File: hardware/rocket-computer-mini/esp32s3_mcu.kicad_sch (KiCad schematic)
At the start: 35 parts, among them SW3 R-667995, U11 GD5F2GQ5UEYIGR, U13 W25Q128JVSIQ, U14 479480001, U15 ESP32-S3RH2, Y1 ABS07-32.768KHZ-T, Y2 ECS-400-10-37B2-CKY-TR

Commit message: hardware: rename the External Connections sheet to Pyro, wire up the 3D models
Two changes that both needed the KiCad session closed.

The External Connections sheet becomes Pyro, in pyro.kicad_sch. The old name
described a sheet that carried the expansion header, camera, servo and piezo
alongside the pyro channels; all of those were removed during the reduction, so
the sheet now carries the four pyro channels and little else. Renamed in the root
schematic, in the project file's sheet list, and across 78 footprint sheetname
and sheetfile properties in the PCB, with the file moved to match.

The two 3D models added earlier are now referenced from their footprints, at
zero offset and rotation -- both were drawn at the footprint origin so they need
no transform. Paths resolve through ${KIPRJMOD}/../3dmodels/ like the other 63.

Verified: the netlist exports cleanly at 157 parts and the sheet path now reads
/Pyro/ alongside /Sensors/, /Power/ and /MCU - ESP32-S3/. No reference to the old
name survives anywhere in the board directory.

Note on the DRC numbers, which look alarming and are not from this change: the
board file currently holds zero net declarations and zero track segments, so DRC
reports every connection as missing. The layout has not been resynced since the
processor removal. That is known and separate.

Also corrects the README, which still described the sheet set as it stood at the
fork.

Co-Authored-By: Claude Opus 5 <noreply@anthropic.com>
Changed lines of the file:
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@@
+		)
+	)
+	(global_label "L_RXEN"
+		(shape input)
+		(at 161.925 86.36 180)
+		(fields_autoplaced yes)
+		(effects
+			(font
+				(size 1.27 1.27)
+			)
+			(justify right)
+		)
+		(property "Intersheetrefs" "${INTERSHEET_REFS}"
+			(at 150.4127 86.36 180)
+			(hide yes)
+			(show_name no)
+			(do_not_autoplace no)
+			(effects
+				(font
+					(size 1.27 1.27)
+				)
+				(justify right)
+			)
 		)
 	)
@@
 			)
 		)
-	)
-	(global_label "L_RXEN"
-		(shape input)
-		(at 161.92499999999998 86.36 180)
-		(fields_autoplaced yes)
-		(effects
-			(font
-				(size 1.27 1.27)
-			)
-			(justify right)
-		)
-		(property "Intersheetrefs" "${INTERSHEET_REFS}"
-			(at 150.4127 86.36 180)
-			(hide yes)
-			(show_name no)
-			(do_not_autoplace no)
-			(effects
-				(font
-					(size 1.27 1.27)
-				)
-				(justify right)
-			)
-		)

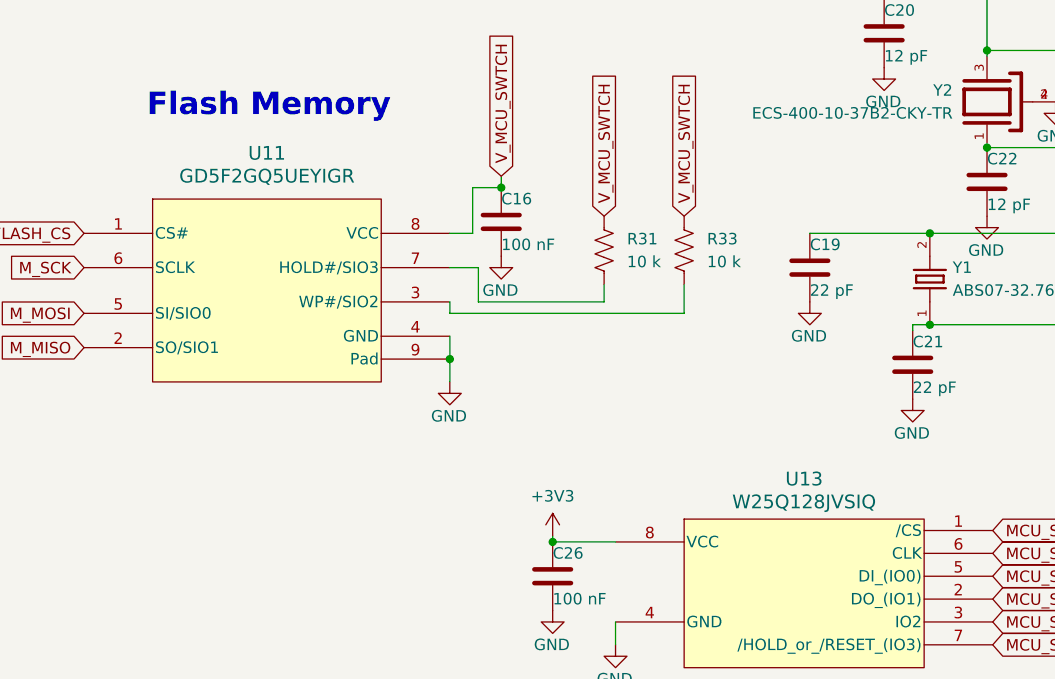
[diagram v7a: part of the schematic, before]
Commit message: hardware: cheaper flash across the fleet, and revs for the boards that had drifted
rocket-computer-mini U11: GD5F2GQ5UEYIGR (2 Gbit) -> GD5F1GQ5UEYIGR (1 Gbit).
Same GigaDevice family, same WSON-8 8x6 land, same pinout and 3.3 V rail, and
the ESP-IDF spi_nand_flash driver already carries device ID 0x51 (1024 blocks =
128 MB) -- a value/MPN change with no layout or firmware work. -$3.81/bd. Also
fixes U11's Datasheet field, which pointed at MX35UF4G24AD-Z4I8, a 1.8 V
Macronix part (flagged as an INFO finding in prefab-review-2026-08-05).

Boot NOR on all six placements: W25Q128JVSIQ -> GD25Q128ESIG (rocket-computer
U13+U16, base-station U1, base-station-mini U1, lora-daughterboard U22,
rocket-computer-mini U13). Identical SOIC-8 208 mil land and standard SPI-NOR
pinout (1 CS#, 2 SO/IO1, 3 WP#/IO2, 4 VSS, 5 SI/IO0, 6 SCLK, 7 HOLD#/IO3,
8 VCC), 2.7-3.6 V, 16 MB, and ESP-IDF has a first-party driver
(spi_flash_chip_gd.c, default y on S3) -- unlike the cheaper Puya part, which
would fall to the generic driver on a boot device. -$1.0471/pc over a 700 pc
line. WSON and 150 mil variants were swept and are 1.5-3.3x dearer for the same
die, so the 208 mil land stays. The shared 3D model is renamed to match; its
geometry is unchanged because the package is identical.

New revs on the boards that had changed since their fab tag without one:
rocket-computer V9 -> V10 and lora-daughterboard V3 -> V4 for this swap, and
gnss-px1105r V1 -> V2 for changes that predate it -- 8a95e02 refilled zones to
clear a 3V3-to-GND short in the stored artwork and da39e6e moved the board off
the default stackup, neither ever marked with a rev. base-station was already
V6; gnss-sam10m8 and servo-adapter are unchanged since fab; the two mini boards
have never been fabbed.

rocket-computer-mini/bom.csv regenerated from the schematic -- it was still the
parent board's BOM from the fork (243 designators against the schematic's 149;
U16 listed as a W25Q128 when it is the E220 radio; U5, the on-board GNSS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
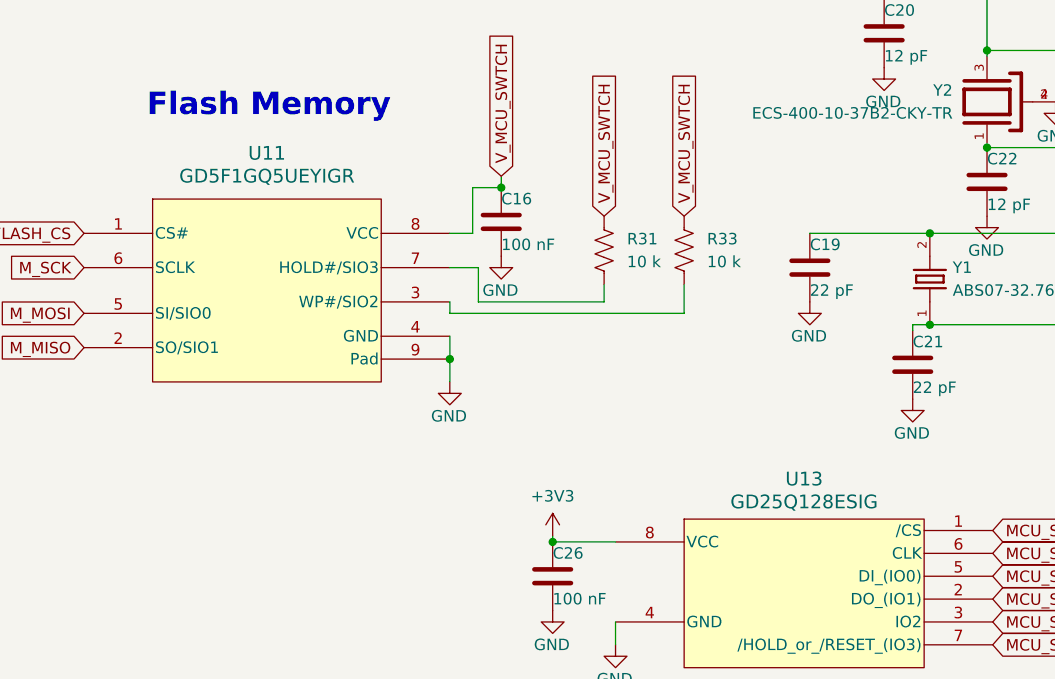
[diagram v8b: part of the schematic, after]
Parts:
- U11: value GD5F2GQ5UEYIGR -> GD5F1GQ5UEYIGR; MPN GD5F2GQ5UEYIGR -> GD5F1GQ5UEYIGR
- U13: value W25Q128JVSIQ -> GD25Q128ESIG; MPN W25Q128JVSIQ -> GD25Q128ESIG; Mfr Winbond -> GigaDevice
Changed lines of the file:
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@@
 			)
 		)
-		(property "Value" "W25Q128JVSIQ"
+		(property "Value" "GD25Q128ESIG"
 			(at 106.68 100.33 0)
 			(show_name no)
@@
 			)
 		)
-		(property "MPN" "W25Q128JVSIQ"
+		(property "MPN" "GD25Q128ESIG"
 			(at 62.865 109.855 0)
 			(hide yes)
@@
 			)
 		)
-		(property "Mfr" "Winbond"
+		(property "Mfr" "GigaDevice"
 			(at 62.865 109.855 0)
 			(hide yes)
@@
 			)
 		)
-		(property "Value" "GD5F2GQ5UEYIGR"
+		(property "Value" "GD5F1GQ5UEYIGR"
 			(at 46.99 64.135 0)
 			(show_name no)
@@
 			)
 		)
-		(property "Datasheet" "MX35UF4G24AD-Z4I8"
+		(property "Datasheet" "GD5F1GQ5UEYIGR"
 			(at 35.052 55.753 0)
 			(hide yes)
@@
 			)
 		)
-		(property "MPN" "GD5F2GQ5UEYIGR"
+		(property "MPN" "GD5F1GQ5UEYIGR"
 			(at 26.67 70.485 0)
 			(hide yes)
